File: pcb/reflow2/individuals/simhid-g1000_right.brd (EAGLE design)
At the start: 35 x 192 mm, 73 parts, among them J4 PCB-INTERCONNECT, J5 ZX62-B-5PA(33)-FULL, J6 2212S, SW27 SLLB510100-HS, SW28 TS-1109S-B-B, SW29 TS-1109S-B-B, SW30 TS-1109S-B-B, SW31 TS-1109S-B-B, SW32 TS-1109S-B-B, SW33 TS-1109S-B-B, SW34 TS-1109S-B-B, U4 STM32F411CCU, U5 MCP23S18-E/MJ, U6 MCP1703AT-3302E/CB, X1 16MHz/10pF

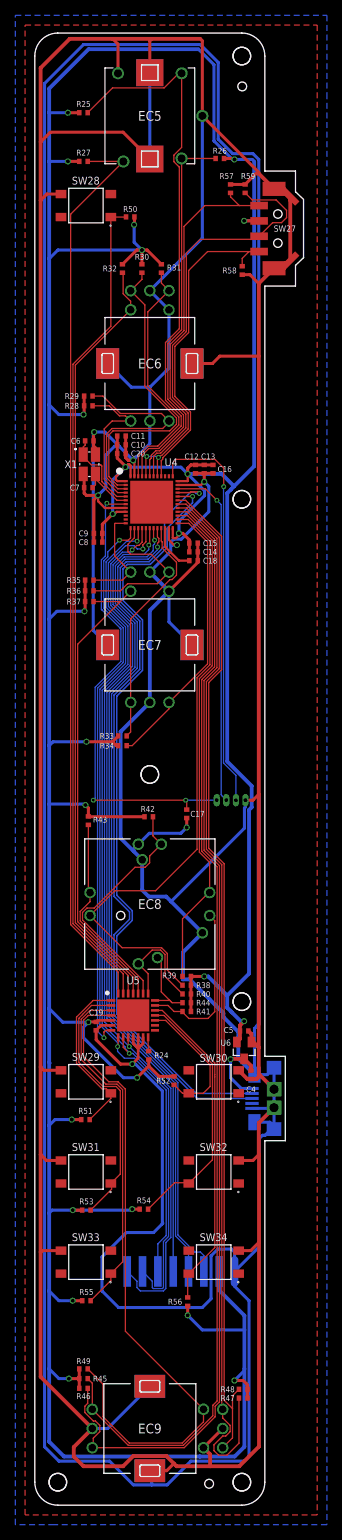
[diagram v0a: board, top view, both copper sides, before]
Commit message: Added vertical USB connector versions
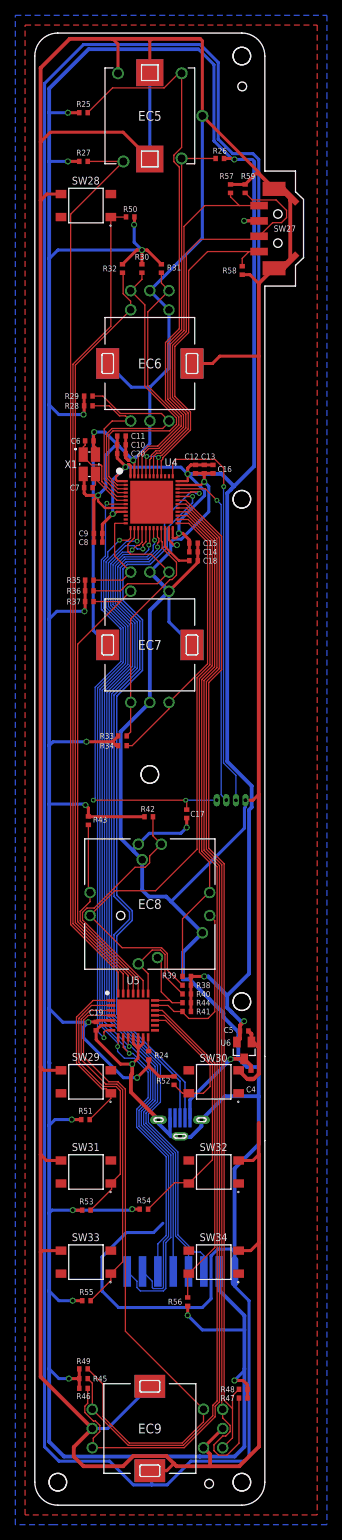
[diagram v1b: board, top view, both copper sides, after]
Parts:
- J5: value ZX62-B-5PA(33)-FULL -> 1051330031-HS; device ZX62-B-5PA(33):ZX62-B-5PA(33)-TRUE-HANDSOLD -> USB-connectors:1051330031-HS
- moved J5 12.8 mm to (18.9, 49.3), turned to 0 degrees
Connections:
- net GND: now also J5.G1, J5.G2, J5.G3; no longer J5.10, J5.11, J5.6, J5.7, J5.8, J5.9
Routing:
- net GND: track 1311.6 -> 1300.4 mm
- net USB_D+: track 104.6 -> 99.0 mm
- net USB_D-: track 101.0 -> 96.3 mm
- net +5V: track 9.48 -> 13.5 mm
- net MISO: track 115.9 -> 117.3 mm
- net EXT1_CS: track 108.8 -> 110.1 mm
- net SCLK: track 108.0 -> 109.2 mm
- net MOSI: track 116.2 -> 117.4 mm
- net EXT3_CS: track 106.5 -> 107.8 mm
- net EXT2_CS: track 107.6 -> 108.8 mm
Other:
- outline, holes or cut-outs redrawn
